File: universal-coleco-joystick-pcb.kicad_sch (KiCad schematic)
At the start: 46 parts, among them J1 Sanwa Joystick, J2 DE9_Receptacle, J3 Conn_01x09_Socket, J4 Opt'l Numbers, SW1 Arm, SW10 2, SW11 #, SW12 9, SW13 6, SW14 3, SW2 Fire, SW3 *, SW4 7, SW5 1, SW6 4, SW7 0, SW8 8, SW9 5

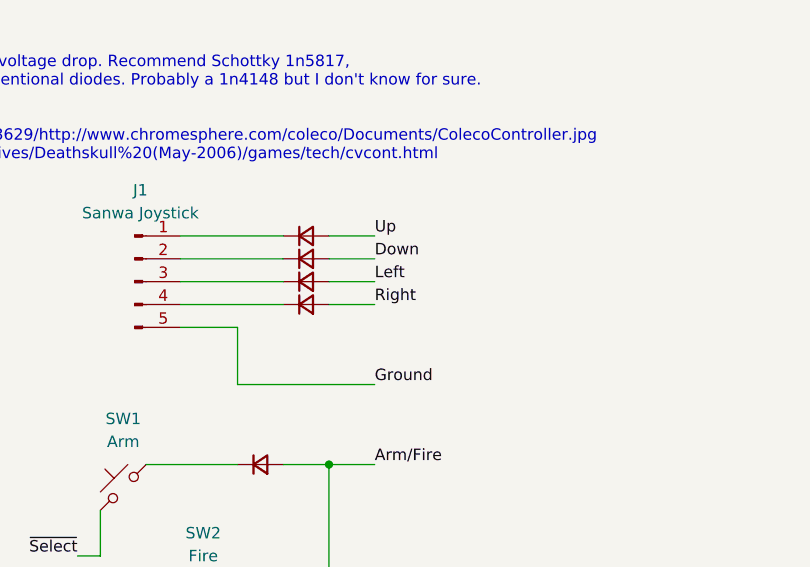
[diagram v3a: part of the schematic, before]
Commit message: UDRL not UDLR joystick error
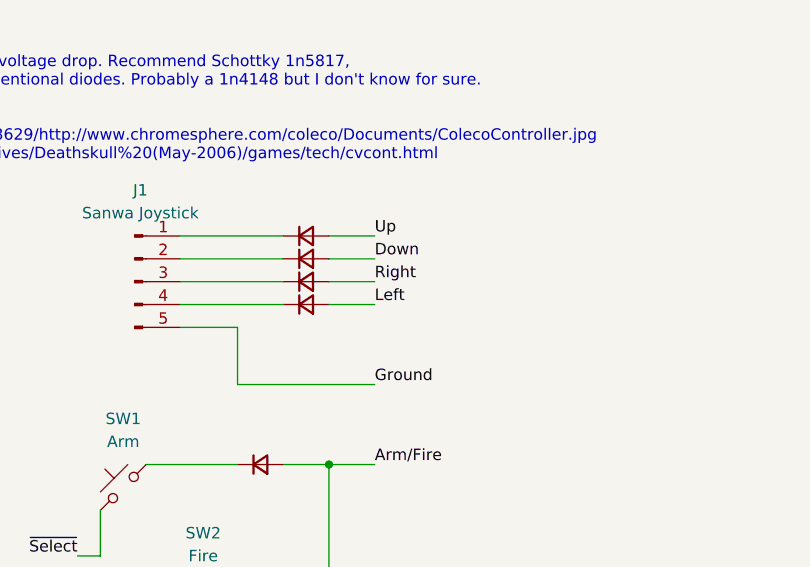
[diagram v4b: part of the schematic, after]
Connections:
- net Left: now also D4.2 (A); no longer D3.2 (A)
- net Right: now also D3.2 (A); no longer D4.2 (A)
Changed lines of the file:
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@@
 	)
 	(label "Left"
-		(at 92.71 58.42 0)
+		(at 92.71 60.96 0)
 		(fields_autoplaced yes)
 		(effects
@@
 	)
 	(label "Right"
-		(at 92.71 60.96 0)
+		(at 92.71 58.42 0)
 		(fields_autoplaced yes)
 		(effects

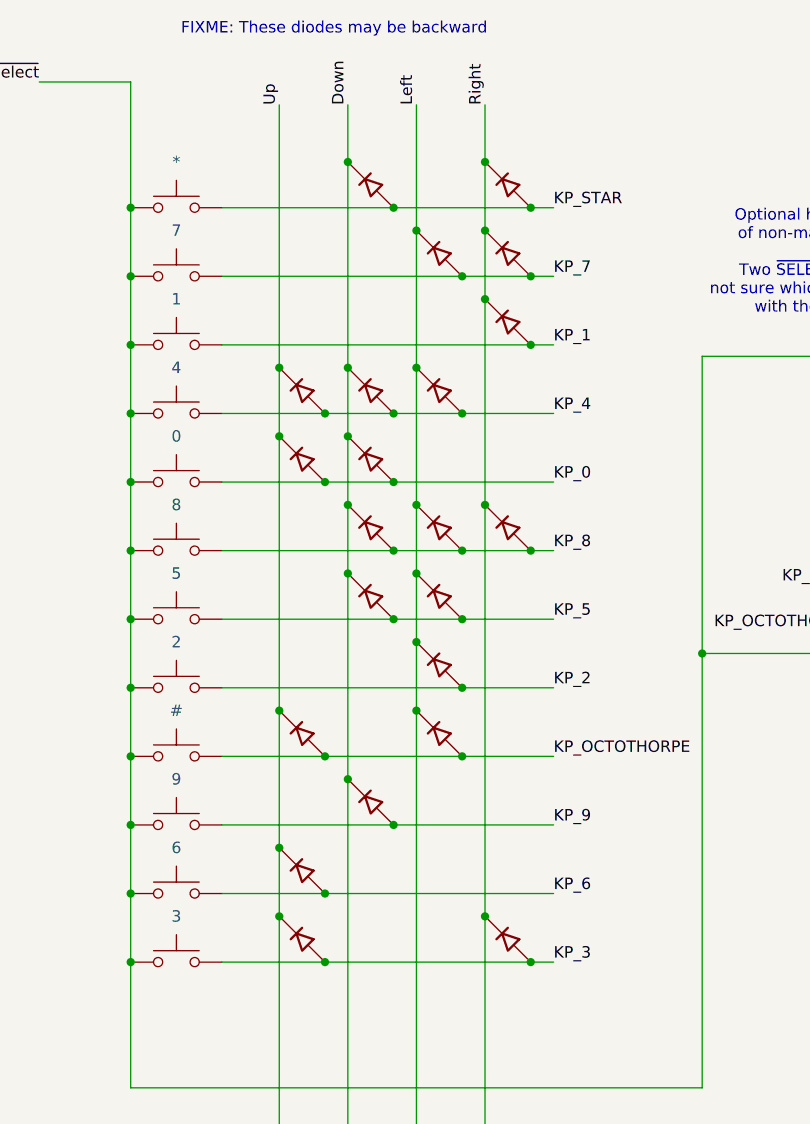
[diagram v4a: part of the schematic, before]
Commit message: Diodes flipped, board shrunk below 100x100
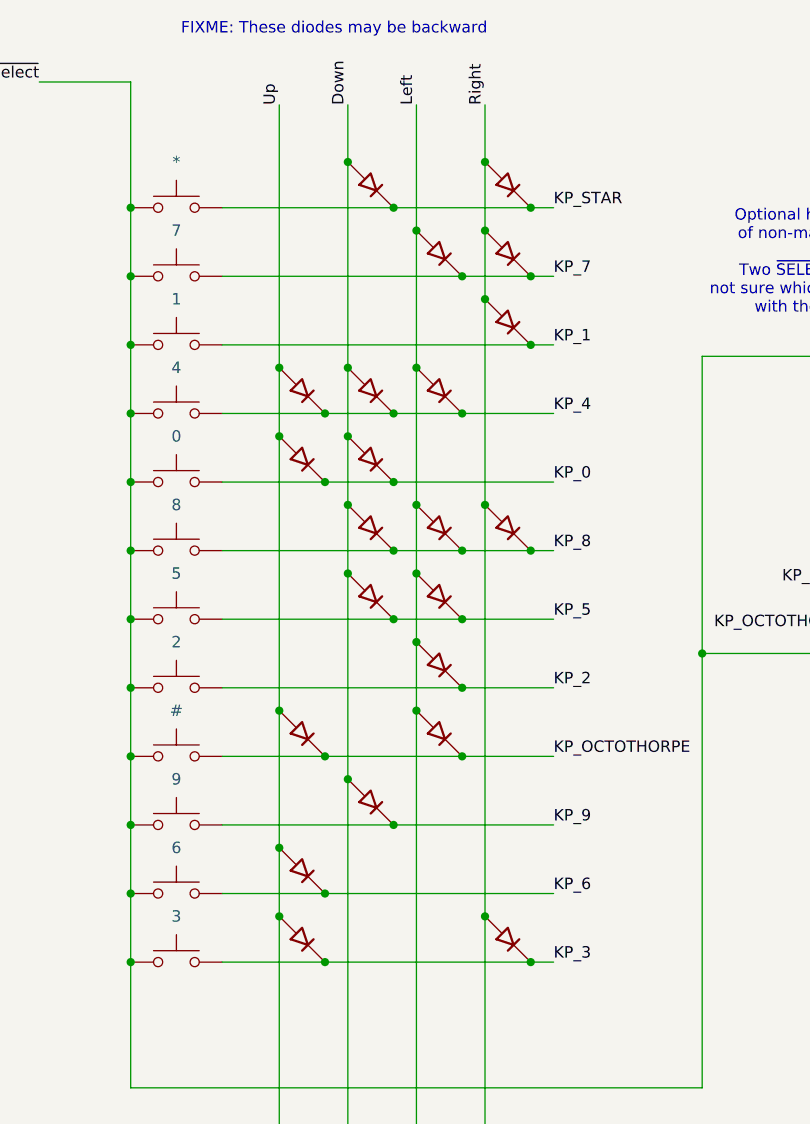
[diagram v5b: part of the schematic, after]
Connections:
- net Down: now also D13.2 (A), D16.2 (A), D17.2 (A), D20.2 (A), D25.2 (A), D7.2 (A); no longer D13.1 (K), D16.1 (K), D17.1 (K), D20.1 (K), D25.1 (K), D7.1 (K)
- net KP_0: now also D15.1 (K), D16.1 (K); no longer D15.2 (A), D16.2 (A)
- net KP_1: now also D11.1 (K); no longer D11.2 (A)
- net KP_2: now also D22.1 (K); no longer D22.2 (A)
- net KP_3: now also D27.1 (K), D28.1 (K); no longer D27.2 (A), D28.2 (A)
- net KP_4: now also D12.1 (K), D13.1 (K), D14.1 (K); no longer D12.2 (A), D13.2 (A), D14.2 (A)
- net KP_5: now also D20.1 (K), D21.1 (K); no longer D20.2 (A), D21.2 (A)
- net KP_6: now also D26.1 (K); no longer D26.2 (A)
- net KP_7: now also D10.1 (K), D9.1 (K); no longer D10.2 (A), D9.2 (A)
- net KP_8: now also D17.1 (K), D18.1 (K), D19.1 (K); no longer D17.2 (A), D18.2 (A), D19.2 (A)
- net KP_9: now also D25.1 (K); no longer D25.2 (A)
- net KP_OCTOTHORPE: now also D23.1 (K), D24.1 (K); no longer D23.2 (A), D24.2 (A)
- net KP_STAR: now also D7.1 (K), D8.1 (K); no longer D7.2 (A), D8.2 (A)
- net Left: now also D14.2 (A), D18.2 (A), D21.2 (A), D22.2 (A), D24.2 (A), D9.2 (A); no longer D14.1 (K), D18.1 (K), D21.1 (K), D22.1 (K), D24.1 (K), D9.1 (K)
- net Right: now also D10.2 (A), D11.2 (A), D19.2 (A), D28.2 (A), D8.2 (A); no longer D10.1 (K), D11.1 (K), D19.1 (K), D28.1 (K), D8.1 (K)
- net Up: now also D12.2 (A), D15.2 (A), D23.2 (A), D26.2 (A), D27.2 (A); no longer D12.1 (K), D15.1 (K), D23.1 (K), D26.1 (K), D27.1 (K)
